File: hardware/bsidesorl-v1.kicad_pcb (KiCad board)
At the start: 2 copper layers, 92 x 63.4 mm, 28 parts, among them J1 Simple_Addon_v2, U1 CH32V003F4P6

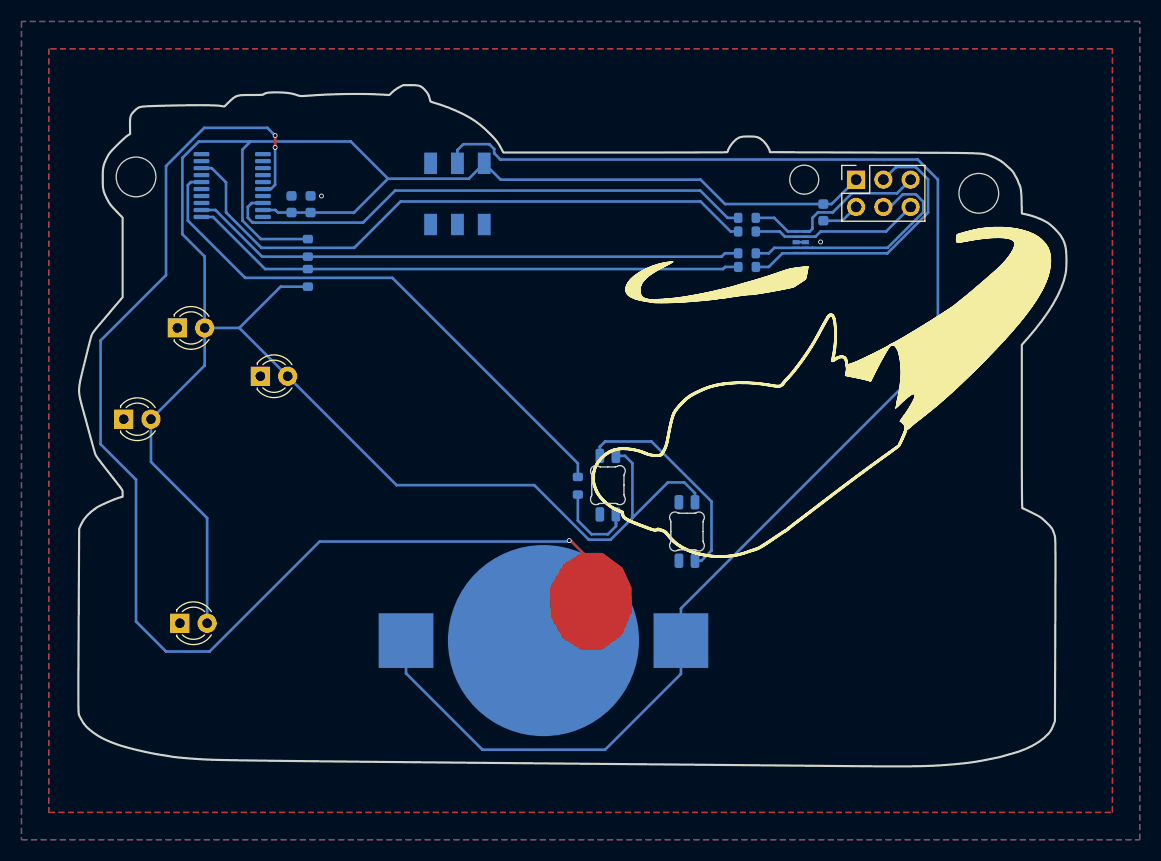
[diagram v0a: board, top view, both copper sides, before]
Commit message: Post-prototype overhaul
* Switch from 1x CR2032 to 2x AAs for power
* Add a switching-mode boost circuit to get a real 3.3v rail
* Add a 3rd SK6812 (scanning LED)
* Add instructions to silkscreen
* Add full-color UV art
* Add current-limiting resistors for each self-blinking LED
* Move SAO tether hole further from SAO connector
* Move one of the self-blinking LEDs to the top of the "space needle"
* Make each self-blinking LED controllable by a GPIO pin
* Switch is now not on the power path but instead controls the boost IC's EN pin
* Almost completely re-did PCB layout
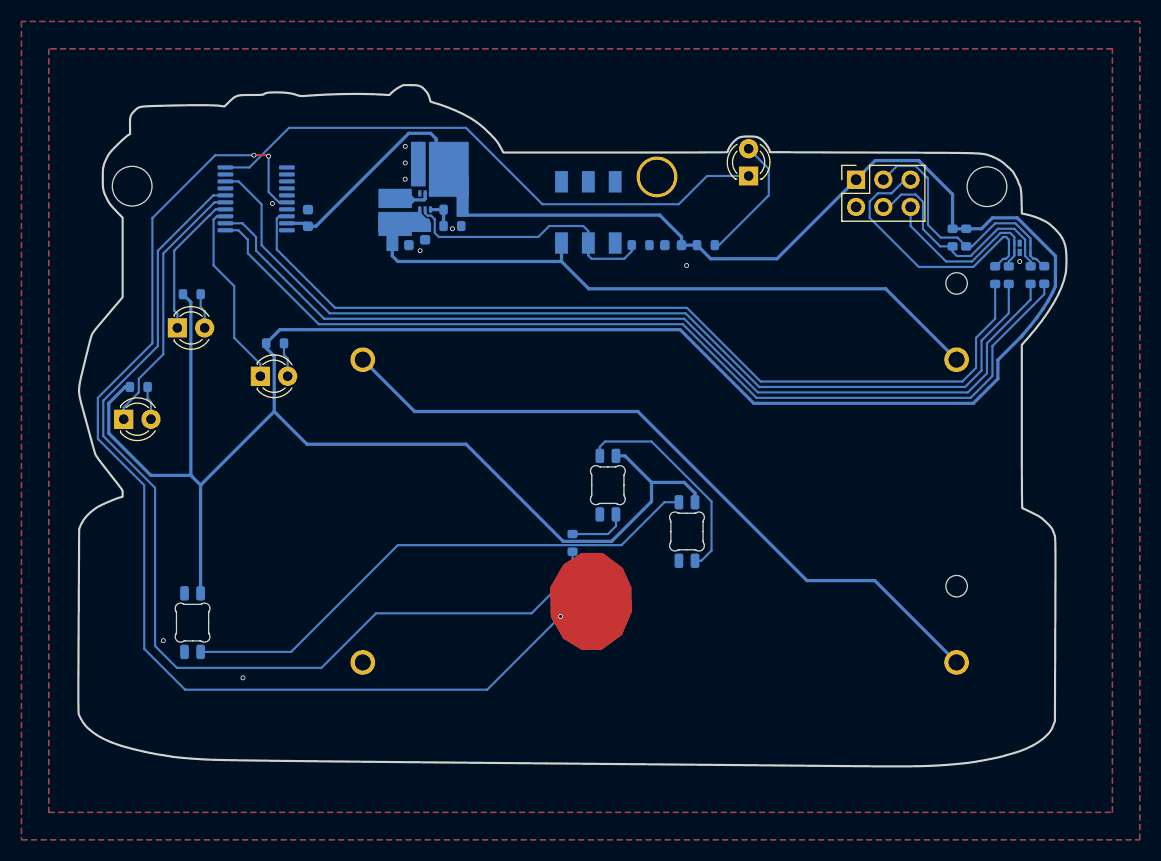
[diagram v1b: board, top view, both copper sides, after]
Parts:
- removed ?: , 
- removed the G*** at (144.4, 99.1) (x2)
- removed the REF** at (183.1, 77.0)
- removed the REF** at (166.9, 75.7)
- added BT2: 1x AA, footprint:BAT-TH_BH-AA-A5BJ012, B.Cu at (153.4, 120.7)
- added C4: 22uF, Capacitor_SMD:C_0603_1608Metric, B.Cu at (131.8, 74.2)
- added C5: 22uF, Capacitor_SMD:C_0603_1608Metric, B.Cu at (131.8, 72.6)
- added C6: 100nF, Capacitor_SMD:C_0603_1608Metric, B.Cu at (120.7, 79.3)
- added C7: 2.2uF, Capacitor_SMD:C_0603_1608Metric, B.Cu at (154.7, 81.8)
- added D8: SK6812MINI-E, LED_SMD:LED_SK6812MINI-E_3.2x2.8mm_P1.5mm_ReverseMount, B.Cu at (109.9, 116.9)
- added HOLE1: LanyardHole, , F.Cu at (183.9, 76.3)
- added HOLE2: LanyardHole, , F.Cu at (104.3, 76.3)
- added L1: 2.2uH, footprint:IND-SMD_L3.5-W3.0, B.Cu at (128.8, 78.7)
- added R10: 470R, Resistor_SMD:R_0603_1608Metric, B.Cu at (104.9, 95.0)
- added R11: 470R, Resistor_SMD:R_0603_1608Metric, B.Cu at (117.6, 90.9)
- added R12: 10K, PCM_JLCPCB:R_0603, B.Cu at (182.0, 81.1)
- added R13: 10K, PCM_JLCPCB:R_0603, B.Cu at (180.7, 81.1)
- added R14: 1M, Resistor_SMD:R_0603_1608Metric, B.Cu at (151.6, 81.8)
- added R8: 470R, Resistor_SMD:R_0603_1608Metric, B.Cu at (157.7, 81.8)
- added R9: 470R, Resistor_SMD:R_0603_1608Metric, B.Cu at (109.8, 86.4)
- added REF**: TetherHole, sao:TetherHole, F.Cu at (153.2, 75.4)
- added U2: TPS61023DRLR, footprint:SOT-563_L1.6-W1.2-P0.50-LS1.6-BR, B.Cu at (131.6, 77.7)
- BT1: value CR2032 -> 1x AA; footprint Battery:BatteryHolder_Keystone_3002_1x2032 -> footprint:BAT-TH_BH-AA-A5BJ012
- C1: value 100nF -> 22uF
- C2: value 10uF -> 100nF
- C3: value 2.2uF -> 22uF
- D1: renamed from D2; value Fast Blink 3mm LED -> Breathing 3mm LED
- D2: renamed from D1; value Breathing 3mm LED -> Fast Blink 3mm LED
- J1: value Simple_Addon_v2 -> SAO Connector
- R1: value 10K -> 453K; footprint PCM_JLCPCB:R_0603 -> Resistor_SMD:R_0603_1608Metric
- R2: value 10K -> 100K; footprint PCM_JLCPCB:R_0603 -> Resistor_SMD:R_0603_1608Metric
- U1: value CH32V003F4P6 -> CH32V003
- moved D1 67.4 mm to (161.7, 75.3), turned to 90 degrees
- moved C3 37.0 mm to (131.8, 75.7), turned to 180 degrees
- moved BT1 28.3 mm to (153.4, 92.5)
- moved R6 27.7 mm to (189.2, 84.6), turned to 90 degrees
- moved R5 26.5 mm to (188.0, 84.6), turned to 90 degrees
- moved R4 24.7 mm to (185.9, 84.6), turned to 90 degrees
- moved R3 23.7 mm to (184.7, 84.6), turned to -90 degrees
- moved D5 20.4 mm to (186.9, 82.0), turned to 0 degrees
- moved R1 14.9 mm to (134.1, 78.5), turned to 180 degrees
- moved R2 13.6 mm to (134.1, 80.0), turned to 0 degrees
- moved S1 12.3 mm to (146.8, 78.7)
- moved C2 11.0 mm to (131.6, 80.5), turned to -90 degrees
- moved C1 10.9 mm to (129.3, 81.8), turned to 0 degrees
- moved R7 5.34 mm to (145.3, 109.5), turned to 90 degrees
- moved U1 2.55 mm to (115.8, 77.5)
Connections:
- BT1 pad 1: Net-(BT1-+) -> VBAT
- BT1 pad 2: GND -> Net-(BT1-Pad2)
- C1 pad 1: GND -> VBAT
- C1 pad 2: VCC -> GND
- C2 pad 1: VCC -> VBAT
- C3 pad 1: VCC -> +3.3V
- D1 pad 1: GND -> ~{LED1_EN}
- D1 pad 2: VCC -> Net-(D1-A)
- D2 pad 1: GND -> ~{LED2_EN}
- D2 pad 2: VCC -> Net-(D2-A)
- D3 pad 1: GND -> ~{LED3_EN}
- D3 pad 2: VCC -> Net-(D3-A)
- D4 pad 1: GND -> ~{LED4_EN}
- D4 pad 2: VCC -> Net-(D4-A)
- D6 pad 3: VCC -> +3.3V
- D7 pad 3: VCC -> +3.3V
- D7 pad 4: unconnected-(D7-DOUT-Pad4) -> Net-(D7-DOUT)
- J1 pad 1: VCC -> +3.3V
- R1 pad 1: VCC -> +3.3V
- R1 pad 2: MCU_SDA -> Net-(U2-FB)
- R2 pad 1: VCC -> Net-(U2-FB)
- R2 pad 2: MCU_SCL -> GND
- S1 pad 1: VCC -> unconnected-(S1-Pad1)
- S1 pad 2: Net-(BT1-+) -> unconnected-(S1-Pad2)
- S1 pad 4: unconnected-(S1-Pad4) -> GND
- S1 pad 5: unconnected-(S1-Pad5) -> Net-(U2-EN)
- S1 pad 6: unconnected-(S1-Pad6) -> VBAT
- U1 pad 13: unconnected-(U1-PC3-Pad13) -> ~{LED4_EN}
- U1 pad 14: unconnected-(U1-PC4-Pad14) -> ~{LED2_EN}
- U1 pad 15: unconnected-(U1-PC5-Pad15) -> ~{LED3_EN}
- U1 pad 20: unconnected-(U1-PD3-Pad20) -> ~{LED1_EN}
- U1 pad 9: VCC -> +3.3V
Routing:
- net +3.3V: track 0.00 -> 284.2 mm
- net VCC: track 216.1 -> 0.00 mm
- net Net-(BT1-+): track 138.3 -> 0.00 mm
- net Net-(BT1-Pad2): track 0.00 -> 67.0 mm
- net VBAT: track 0.00 -> 63.5 mm
- net ~{LED1_EN}: track 0.00 -> 54.3 mm
- net Net-(D7-DOUT): track 0.00 -> 50.3 mm
- net WS2812_DATA: track 51.6 -> 94.7 mm
- net MCU_SDA: track 52.1 -> 90.1 mm
- net MCU_SCL: track 51.9 -> 88.9 mm
- net MCU_RX_DBG: track 57.6 -> 90.3 mm
- net MCU_TX: track 50.7 -> 83.2 mm
- net Net-(U2-EN): track 0.00 -> 26.0 mm
- net ~{LED3_EN}: track 0.00 -> 24.7 mm
- net ~{LED4_EN}: track 0.00 -> 17.6 mm
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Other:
- board text added: "3V3"
- board text added: "4 LEDs: square pad = shorter pin and flat side"
- board text added: "Art by Shep"
- board text added: "GND"
- board text added: "OFF"
- board text added: "ON"
- board text added: "PCB by kcolley"
- board text added: "RXD"
- board text added: "SAO connector should have notch facing up!"
- board text added: "SCL"
- board text added: "SDA"
- board text added: "TXD"
- board text removed: "BSides Orlando Badge 2026 DVT R0 - 08/2026 kcolley joehacksalot"
- board text removed: "SAO tether"

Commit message: Final schematic, ready to order
* Switched from 2x AAs to 1x AAA
* Switched boost IC from TPS61023 to TPS61021A for lower VIN requirement due to single cell design change
* Added a second capacitive touch area just because
* Finalize back silkscreen
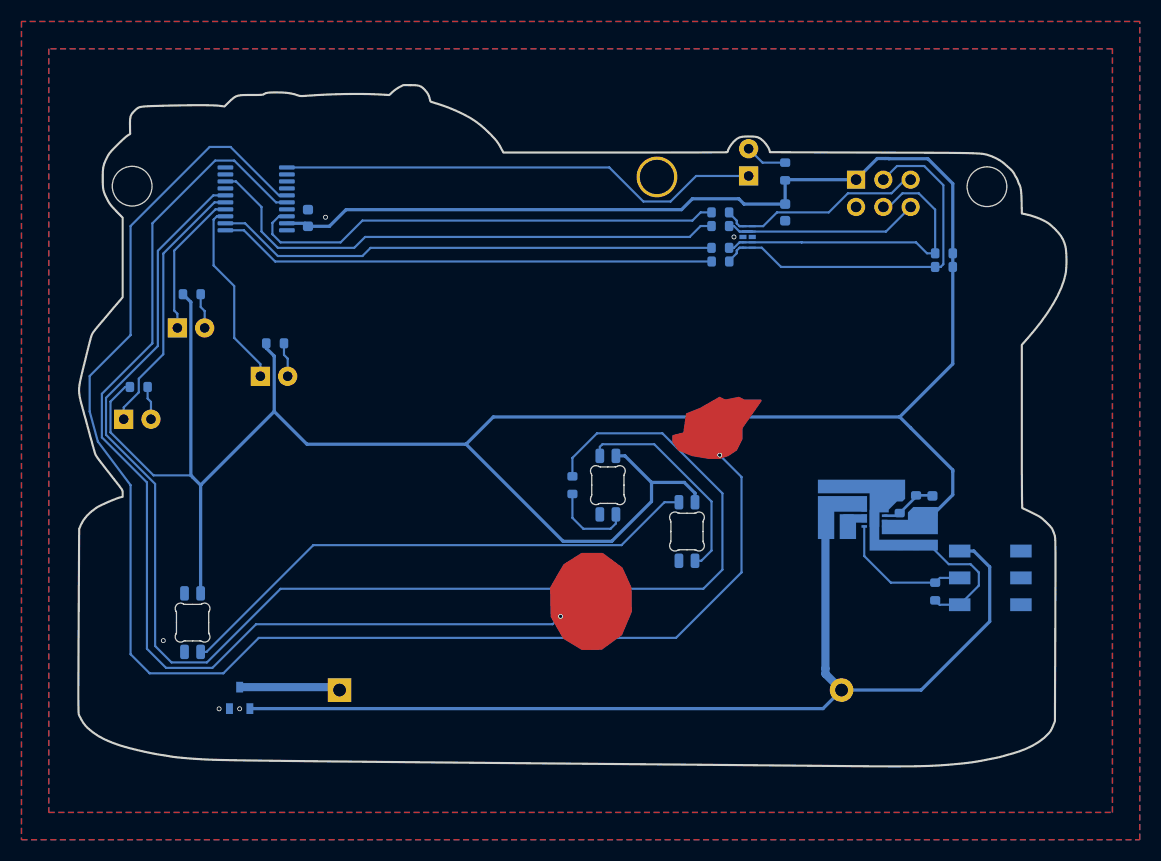
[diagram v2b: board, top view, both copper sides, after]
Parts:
- removed BT2: 1x AA, footprint:BAT-TH_BH-AA-A5BJ012
- removed the C1 at (129.3, 81.8)
- removed the R14 at (151.6, 81.8)
- removed S1: MST22D18G2_125, footprint:SW-SMD_MST22D18G2
- added Q1: SI2302S, footprint:SOT-23-3_L2.9-W1.3-P1.90-LS2.4-BR, B.Cu at (114.3, 124.0)
- added R3: 100K, Resistor_SMD:R_0603_1608Metric, B.Cu at (175.8, 105.9)
- added SW1: MST22D18G2_125, footprint:SW-SMD_MST22D18G2, B.Cu at (184.2, 112.8)
- BT1: value 1x AA -> 1x AAA; footprint footprint:BAT-TH_BH-AA-A5BJ012 -> footprint:BAT-TH_BH-AAA-1X
- C2: value 100nF -> 22uF
- C3: value 22uF -> 10pF
- L1: value 2.2uH -> 1uH; footprint footprint:IND-SMD_L3.5-W3.0 -> Inductor_SMD:L_1008_2520Metric
- R1: value 453K -> 1M
- R2: value 100K -> 316K
- U1: value CH32V003 -> CH32V003F4P6
- U2: value TPS61023DRLR -> TPS61021ADSGR; footprint footprint:SOT-563_L1.6-W1.2-P0.50-LS1.6-BR -> footprint:WSON-8_L2.0-W2.0-P0.50-TL-EP
- moved C5 58.2 mm to (177.3, 109.0), turned to -90 degrees
- moved R1 57.3 mm to (179.1, 114.0), turned to -90 degrees
- moved C4 56.1 mm to (175.8, 109.0), turned to -90 degrees
- moved C3 55.9 mm to (178.8, 105.9), turned to 90 degrees
- moved U2 51.2 mm to (173.4, 107.2), turned to 180 degrees
- moved L1 50.5 mm to (169.9, 108.0), turned to 0 degrees
- moved R2 50.4 mm to (177.3, 105.9), turned to 90 degrees
- moved C2 44.6 mm to (168.9, 104.9), turned to 90 degrees
- moved BT1 31.4 mm to (147.1, 123.2)
- moved R9 30.2 mm to (159.1, 83.3), turned to 0 degrees
- moved R8 29.0 mm to (159.1, 82.0), turned to 0 degrees
- moved R7 27.3 mm to (159.1, 80.0), turned to 0 degrees
- moved R6 26.3 mm to (159.1, 78.7), turned to 180 degrees
- moved D4 25.4 mm to (161.6, 81.0), turned to -90 degrees
- moved C6 10.9 mm to (165.1, 78.7), turned to -90 degrees
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- renumbered C6 to C1, C7 to C6, D6 to D1, D7 to D2, D8 to D3, D5 to D4, D1 to D5, D2 to D6, D3 to D7, D4 to D8, R8 to R10, R9 to R11, R10 to R12, R11 to R13, R13 to R14, R7 to R4, R12 to R5, R3 to R6, R4 to R7, R5 to R8, R6 to R9
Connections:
- net CAP_TOUCH renamed /CAP_TOUCH_FINGERPRINT
- C3 pad 2: GND -> Net-(U2-FB)
- L1 pad 2: Net-(U2-SW) -> Net-(L1-Pad2)
- R1 pad 1: +3.3V -> Net-(U2-EN)
- R1 pad 2: Net-(U2-FB) -> GND
- R2 pad 1: Net-(U2-FB) -> +3.3V
- R2 pad 2: GND -> Net-(U2-FB)
- U1 pad 1: unconnected-(U1-PD4-Pad1) -> ~{LED1_EN}
- U1 pad 20: ~{LED1_EN} -> unconnected-(U1-PD3-Pad20)
- U1 pad 5: unconnected-(U1-PA1-Pad5) -> /CAP_TOUCH_CHOMPY
- U2 pad 1: Net-(U2-FB) -> GND
- U2 pad 2: Net-(U2-EN) -> Net-(U2-FB)
- U2 pad 3: VBAT -> +3.3V
- U2 pad 4: GND -> +3.3V
- U2 pad 5: Net-(U2-SW) -> Net-(U2-EN)
- U2 pad 6: +3.3V -> Net-(L1-Pad2)
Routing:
- net /CAP_TOUCH_CHOMPY: track 0.00 -> 135.3 mm, vias 0 -> 1
- net Net-(BT1--): track 67.0 -> 9.16 mm
- net MCU_SDA: track 90.1 -> 46.5 mm
- net MCU_SCL: track 88.9 -> 46.8 mm
- net MCU_RX_DBG: track 90.3 -> 50.0 mm
- net MCU_TX: track 83.2 -> 45.0 mm
- net WS2812_DATA: track 94.7 -> 132.2 mm
- net VBAT: track 63.5 -> 96.6 mm
- net +3.3V: track 284.2 -> 256.9 mm
- net Net-(U2-EN): track 26.0 -> 12.9 mm
- net GND: track 0.00 -> 11.5 mm, vias 10 -> 5
- net /SAO_SDA: track 24.8 -> 35.7 mm
- net ~{LED1_EN}: track 54.3 -> 45.3 mm
- net Net-(D5-A): track 12.1 -> 3.94 mm
- net /SAO_SCL: track 22.0 -> 29.9 mm
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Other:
- board text added: "CH32V003"
- board text added: "SAO connector should have notch facing up! 4 LEDs: square pad = shorter pin and flat side"
- board text added: "wyd?"
- board text removed: "4 LEDs: square pad = shorter pin and flat side"
- board text removed: "SAO connector should have notch facing up!"
